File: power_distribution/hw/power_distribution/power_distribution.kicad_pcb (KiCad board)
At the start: 2 copper layers, 52 parts, among them J1 XT30-M_Ver, J2 JST-PH_01x02, J3 JST-PH_01x02, J4 JST-PH_01x02, Q1 60Vds, U1 LMR51635XFDDCR, U2 AP63205WU-7, U3 AP63203WU-7

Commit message: First PCB draft
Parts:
- added C24: 0.1uF, Capacitor_SMD:C_0603_1608Metric_Pad1.08x0.95mm_HandSolder, F.Cu at (93.5, 27.6)
- added D9: 3.3Vrwm, ESD5Z5.0T1G:SOD-523_0P9X1P3_ONS, F.Cu at (94.7, 29.1)
- added F5: 0.5A 16V, 0ZCH0050FF2G:0ZCH_BEL, F.Cu at (84.7, 31.6)
- added F6: 0.5A 16V, 0ZCH0050FF2G:0ZCH_BEL, F.Cu at (95.3, 31.6)
- added J5: JST-PH_01x02, Connector_JST:JST_PH_S2B-PH-K_1x02_P2.00mm_Horizontal, F.Cu at (94.5, 24.9)
- added R7: 100k, Resistor_SMD:R_0603_1608Metric_Pad0.98x0.95mm_HandSolder, F.Cu at (31.6, 22.2)
- C3: footprint Capacitor_SMD:CP_Elec_10x10 -> Capacitor_SMD:CP_Elec_8x10
- C5: footprint Capacitor_SMD:CP_Elec_10x10 -> Capacitor_SMD:CP_Elec_6.3x7.7
- C7: footprint Capacitor_SMD:CP_Elec_10x10 -> Capacitor_SMD:CP_Elec_5x5.3
- moved C7 73.3 mm to (90.0, 31.2), turned to 90 degrees
- moved F4 70.8 mm to (94.8, 35.1)
- moved C23 64.1 mm to (94.2, 43.1)
- moved C22 64.0 mm to (94.2, 39.9)
- moved F3 57.1 mm to (71.7, 20.8), turned to 90 degrees
- moved C5 54.7 mm to (74.2, 31.9), turned to -90 degrees
- moved D7 53.3 mm to (85.6, 29.1)
- moved C20 51.6 mm to (81.7, 44.6)
- moved C8 50.9 mm to (86.5, 27.6)
- moved L3 49.4 mm to (88.0, 41.7)
- moved D5 48.3 mm to (71.7, 23.9), turned to 180 degrees
- moved F2 44.8 mm to (58.4, 20.9), turned to 90 degrees
- moved C21 43.2 mm to (82.5, 39.0)
- moved C9 42.4 mm to (25.4, 25.4), turned to 180 degrees
- moved D4 42.1 mm to (58.4, 24.1), turned to 180 degrees
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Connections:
- C7 pad 1: Net-(D8-A) -> /3V3_SPLIT
- C8 pad 1: Net-(D8-A) -> Net-(J4-Pin_2)
- D7 pad 1: Net-(D8-A) -> Net-(J4-Pin_2)
- D8 pad 2: Net-(D8-A) -> /3V3_SPLIT
- F4 pad 1: Net-(D8-A) -> /3V3_SPLIT
- J4 pad 2: Net-(D8-A) -> Net-(J4-Pin_2)
- U1 pad 2: VBAT -> Net-(U1-EN)

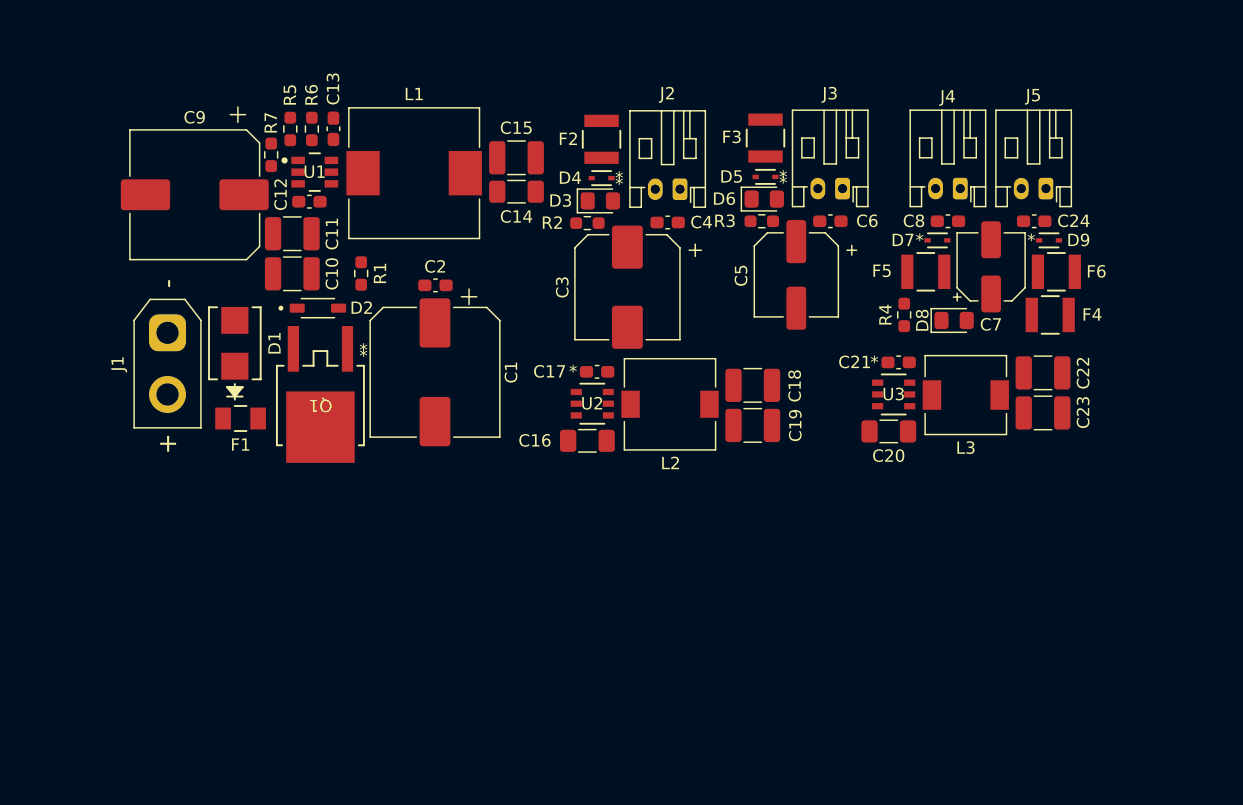
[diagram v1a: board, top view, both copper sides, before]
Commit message: Add test points
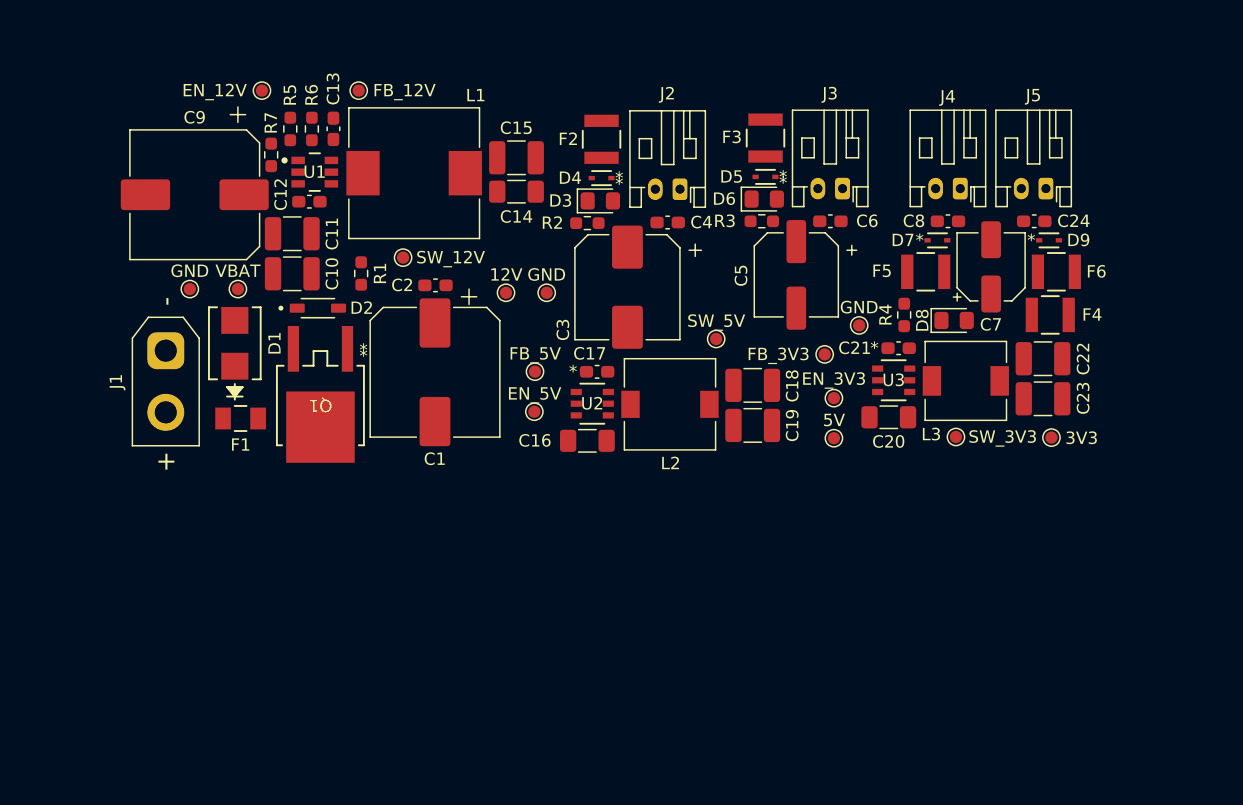
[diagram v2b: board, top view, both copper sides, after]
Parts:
- added 12V: 12V, TestPoint:TestPoint_Pad_D1.0mm, F.Cu at (50.6, 33.4)
- added 3V3: 3V3, TestPoint:TestPoint_Pad_D1.0mm, F.Cu at (94.9, 45.1)
- added 5V: 5V, TestPoint:TestPoint_Pad_D1.0mm, F.Cu at (77.2, 45.1)
- added EN_12V: EN_12V, TestPoint:TestPoint_Pad_D1.0mm, F.Cu at (30.9, 16.9)
- added EN_3V3: EN_3V3, TestPoint:TestPoint_Pad_D1.0mm, F.Cu at (77.2, 41.9)
- added EN_5V: EN_5V, TestPoint:TestPoint_Pad_D1.0mm, F.Cu at (53.0, 43.0)
- added FB_12V: FB_12V, TestPoint:TestPoint_Pad_D1.0mm, F.Cu at (38.7, 16.9)
- added FB_3V3: FB_3V3, TestPoint:TestPoint_Pad_D1.0mm, F.Cu at (76.5, 38.4)
- added FB_5V: FB_5V, TestPoint:TestPoint_Pad_D1.0mm, F.Cu at (53.0, 39.8)
- added GND: GND, TestPoint:TestPoint_Pad_D1.0mm, F.Cu at (25.0, 33.0)
- added GND: GND, TestPoint:TestPoint_Pad_D1.0mm, F.Cu at (79.3, 36.0)
- added GND: GND, TestPoint:TestPoint_Pad_D1.0mm, F.Cu at (54.0, 33.4)
- added SW_12V: SW_12V, TestPoint:TestPoint_Pad_D1.0mm, F.Cu at (42.3, 30.5)
- added SW_3V3: SW_3V3, TestPoint:TestPoint_Pad_D1.0mm, F.Cu at (87.2, 45.0)
- added SW_5V: SW_5V, TestPoint:TestPoint_Pad_D1.0mm, F.Cu at (67.7, 37.1)
- added VBAT: VBAT, TestPoint:TestPoint_Pad_D1.0mm, F.Cu at (28.9, 33.0)
- moved J1 1.46 mm to (23.1, 38.0)
- moved C20 1.15 mm to (81.7, 43.5)
- moved C21 1.15 mm to (82.5, 37.9)
- moved C22 1.15 mm to (94.2, 38.7)
- moved C23 1.15 mm to (94.2, 42.0)
- moved L3 1.15 mm to (88.0, 40.5)
- moved U3 1.15 mm to (82.1, 40.4)

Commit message: Add mounting holes and refactor test points
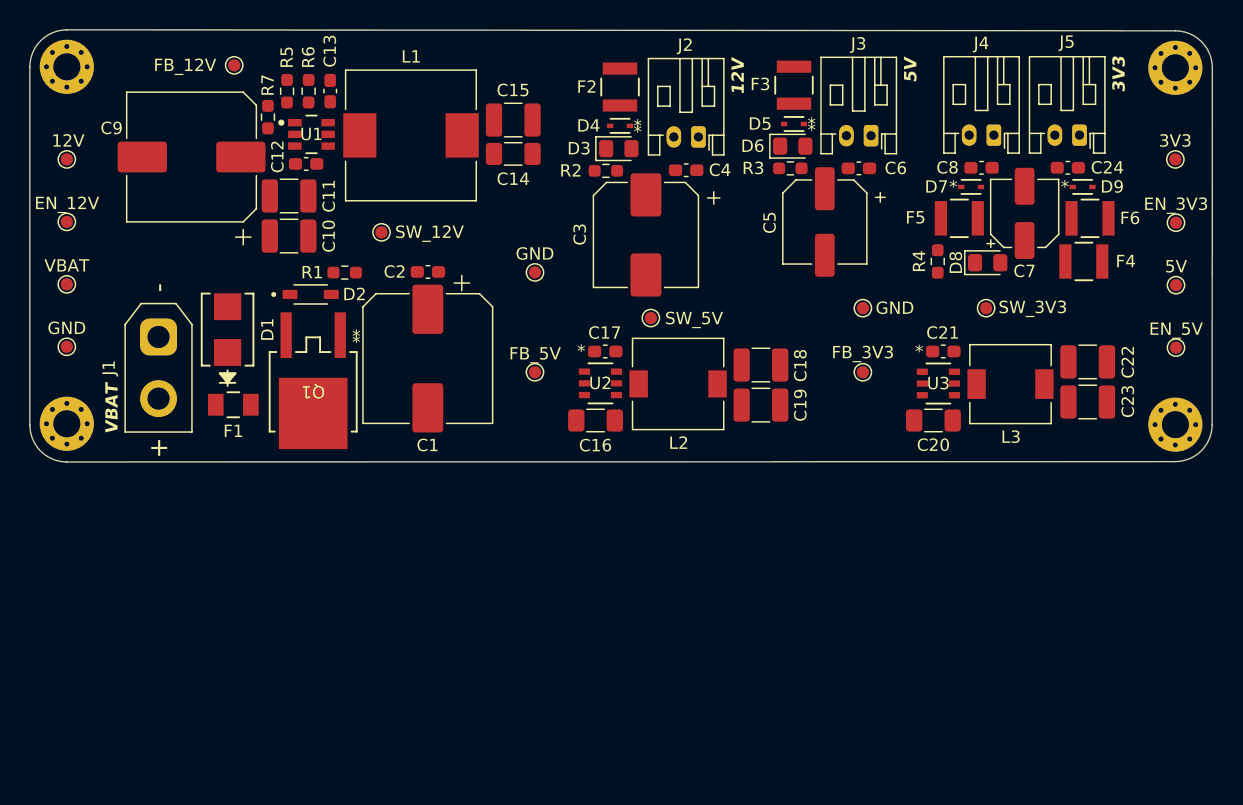
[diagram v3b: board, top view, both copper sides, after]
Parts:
- added H1: MountingHole_Pad, MountingHole:MountingHole_2.2mm_M2_Pad_Via, F.Cu at (15.0, 15.0)
- added H2: MountingHole_Pad, MountingHole:MountingHole_2.2mm_M2_Pad_Via, F.Cu at (105.0, 15.1)
- added H3: MountingHole_Pad, MountingHole:MountingHole_2.2mm_M2_Pad_Via, F.Cu at (15.0, 44.0)
- added H4: MountingHole_Pad, MountingHole:MountingHole_2.2mm_M2_Pad_Via, F.Cu at (105.0, 44.0)
- 12V1: renamed from 12V; footprint TestPoint:TestPoint_Pad_D1.0mm -> test_point_custom:TestPoint_Pad_D1.0mm
- 3V3, EN_3V3, FB_3V3, SW_3V3: footprint TestPoint:TestPoint_Pad_D1.0mm -> test_point_custom:TestPoint_Pad_D1.0mm
- 5V1: renamed from 5V; footprint TestPoint:TestPoint_Pad_D1.0mm -> test_point_custom:TestPoint_Pad_D1.0mm
- EN_12V1: renamed from EN_12V; footprint TestPoint:TestPoint_Pad_D1.0mm -> test_point_custom:TestPoint_Pad_D1.0mm
- EN_5V1: renamed from EN_5V; footprint TestPoint:TestPoint_Pad_D1.0mm -> test_point_custom:TestPoint_Pad_D1.0mm
- FB_12V1: renamed from FB_12V; footprint TestPoint:TestPoint_Pad_D1.0mm -> test_point_custom:TestPoint_Pad_D1.0mm
- FB_5V1: renamed from FB_5V; footprint TestPoint:TestPoint_Pad_D1.0mm -> test_point_custom:TestPoint_Pad_D1.0mm
- GND1, GND2, GND3: renamed from GND; footprint TestPoint:TestPoint_Pad_D1.0mm -> test_point_custom:TestPoint_Pad_D1.0mm
- SW_12V1: renamed from SW_12V; footprint TestPoint:TestPoint_Pad_D1.0mm -> test_point_custom:TestPoint_Pad_D1.0mm
- SW_5V1: renamed from SW_5V; footprint TestPoint:TestPoint_Pad_D1.0mm -> test_point_custom:TestPoint_Pad_D1.0mm
- VBAT1: renamed from VBAT; footprint TestPoint:TestPoint_Pad_D1.0mm -> test_point_custom:TestPoint_Pad_D1.0mm
- moved EN_5V1 52.3 mm to (105.0, 37.8)
- moved 12V1 37.2 mm to (15.0, 22.5)
- moved EN_3V3 31.2 mm to (105.0, 27.7)
- moved 5V1 30.4 mm to (105.0, 32.7)
- moved 3V3 24.7 mm to (105.0, 22.5)
- moved EN_12V1 19.1 mm to (15.0, 27.6)
- moved VBAT1 13.9 mm to (15.0, 32.7)
- moved GND1 11.0 mm to (15.0, 37.7)
- moved SW_3V3 10.7 mm to (89.6, 34.6)
- moved FB_12V1 10.3 mm to (28.6, 14.9)
- moved SW_5V1 5.57 mm to (62.4, 35.4)
- moved D8 5.42 mm to (89.7, 30.9)
- moved F4 5.12 mm to (97.5, 30.8)
- moved F6 5.12 mm to (98.0, 27.3)
- moved C24 5.12 mm to (96.2, 23.2)
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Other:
- board outline added: 95.9 x 35.1 mm
- copper layers 2 -> 4
- board text added: "12V"
- board text added: "3V3"
- board text added: "5V"
- board text added: "VBAT"

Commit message: Trace routes
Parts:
- moved 12V1 35.1 mm to (49.6, 28.4)
- moved D1 7.18 mm to (24.3, 30.2), turned to 180 degrees
- moved R1 6.76 mm to (30.8, 31.6), turned to 180 degrees
- moved EN_12V1 5.07 mm to (15.0, 22.5)
- moved F1 4.33 mm to (25.4, 45.4)
- moved GND2 3.26 mm to (52.0, 34.8)
- moved Q1 3.18 mm to (31.8, 41.4)
- moved D2 3.18 mm to (31.6, 33.5)
- moved C1 3.17 mm to (41.1, 38.7)
- moved C2 3.17 mm to (41.1, 31.7)
- moved VBAT1 2.53 mm to (15.0, 30.1)
- moved FB_5V1 1.72 mm to (52.0, 41.2)
- moved GND3 1.60 mm to (79.6, 36.2)
- moved SW_3V3 1.60 mm to (89.6, 36.2)
- moved FB_3V3 1.20 mm to (79.6, 41.0)
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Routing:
- net 5V_BUS: track 0.00 -> 143.6 mm, vias 0 -> 12
- net 12V_BUS: track 0.00 -> 135.8 mm, vias 0 -> 13
- net GND: track 0.00 -> 127.3 mm, vias 0 -> 42
- net VBAT: track 0.00 -> 68.3 mm, vias 0 -> 2
- net 3V3_BUS: track 0.00 -> 63.1 mm, vias 0 -> 5
- net Net-(U1-EN): track 0.00 -> 21.6 mm, vias 0 -> 2
- net Net-(Q1-D): track 0.00 -> 21.3 mm
- net Net-(U1-SW): track 0.00 -> 16.7 mm
- net /3V3_SPLIT: track 0.00 -> 15.8 mm
- net Net-(D3-A): track 0.00 -> 14.2 mm
- net Net-(D6-A): track 0.00 -> 13.9 mm
- net Net-(J5-Pin_2): track 0.00 -> 9.79 mm
- net Net-(U2-SW): track 0.00 -> 9.72 mm
- net Net-(U1-FB): track 0.00 -> 9.05 mm
- net Net-(U3-SW): track 0.00 -> 8.92 mm
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- added copper zone on F.Cu, net 12V_BUS
- added copper zone on F.Cu, net 3V3_BUS
- added copper zone on F.Cu, net 5V_BUS
- added copper zone on B.Cu, net GND
- added copper zone on F.Cu, net GND
- added copper zone on In1.Cu, net GND
- added copper zone on F.Cu, net Net-(U1-SW)
- added copper zone on F.Cu, net VBAT

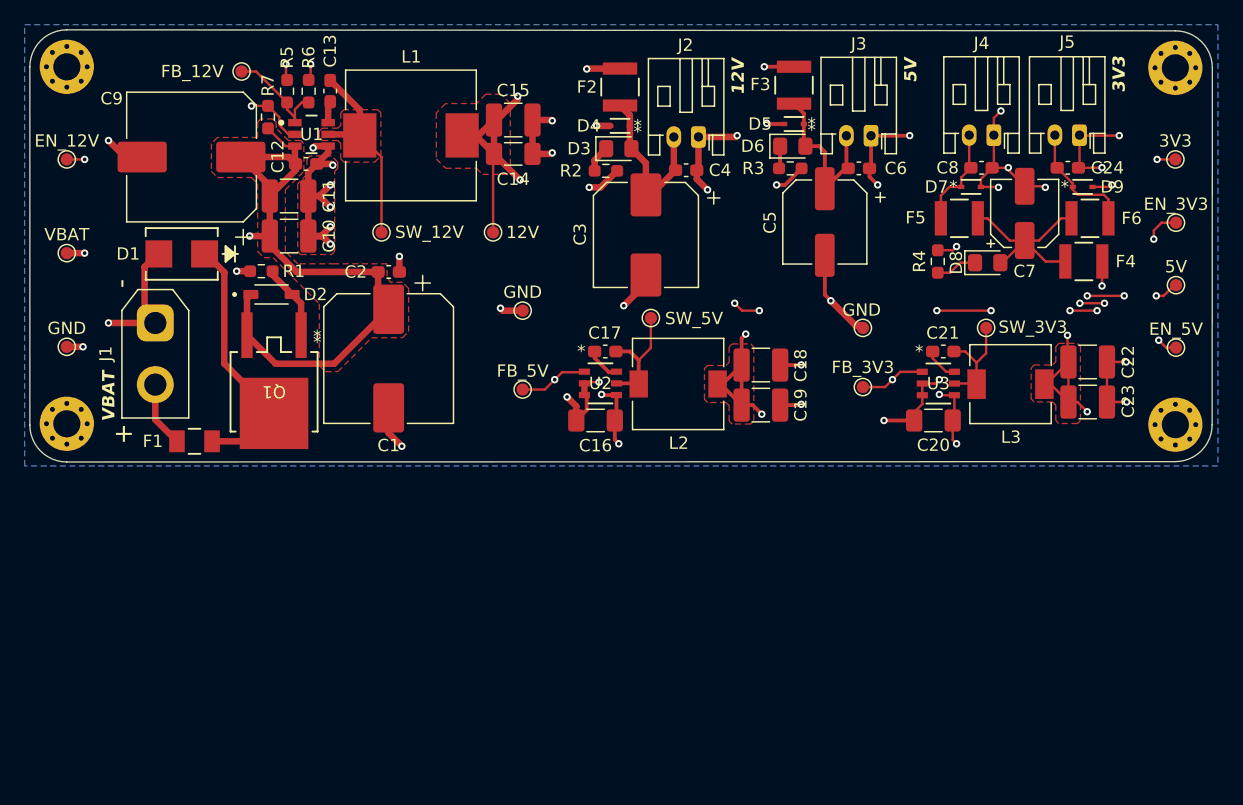
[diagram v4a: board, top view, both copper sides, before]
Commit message: Finish finding last parts and 3D models
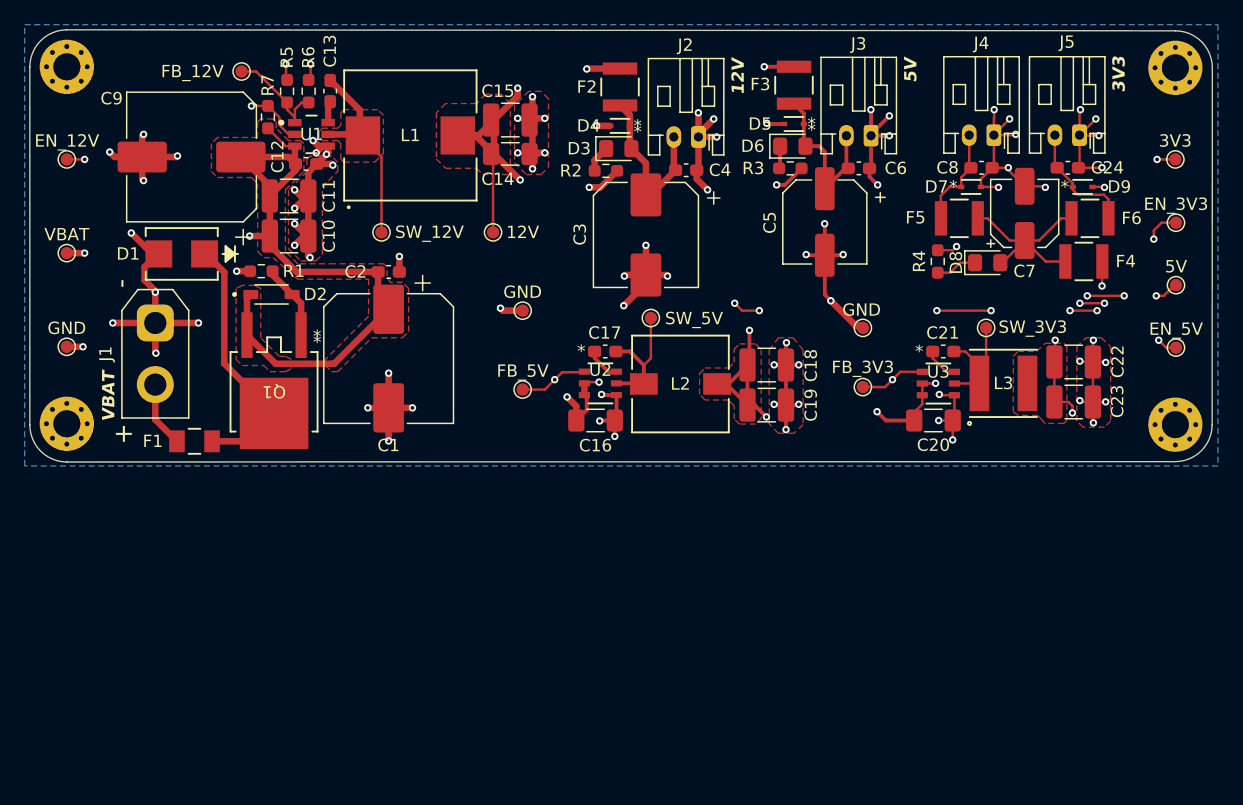
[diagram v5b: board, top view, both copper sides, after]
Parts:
- L1: footprint Inductor_SMD:L_10.4x10.4_H4.8 -> 7447714560:IND_1050P-WE-PD_WRE
- L2: footprint Inductor_SMD:L_7.3x7.3_H4.5 -> 7447779004:IND_7345R_WE-PD_WRE
- L3: footprint Inductor_SMD:L_6.3x6.3_H3 -> 74404052039:IND_WE-LQS_5020_WRE
- moved C22 1.14 mm to (96.7, 39.0)
- moved C23 1.14 mm to (96.7, 42.2)
- moved L3 0.58 mm to (91.0, 40.7)
- moved C18 0.47 mm to (71.8, 39.2)
- moved C19 0.47 mm to (71.8, 42.5)
- moved C14 0.24 mm to (51.0, 22.1)
- moved C15 0.24 mm to (51.0, 19.3)
- moved L2 0.19 mm to (64.8, 40.8)
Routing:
- net GND: track 127.3 -> 190.5 mm, vias 42 -> 83
- net 3V3_BUS: track 63.1 -> 57.1 mm
- net Net-(U3-SW): track 8.92 -> 12.5 mm
- net 5V_BUS: track 143.6 -> 145.2 mm
- net 12V_BUS: track 135.8 -> 135.1 mm
